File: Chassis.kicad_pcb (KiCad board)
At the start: 4 copper layers, 80 x 80.1 mm, 73 parts, among them IC1 LV2862YDDCR, IC2 RT6285GSP, J1 FR_JST, J10 IN_XT30, J11 SWD_IN, J12 Conn_01x08_Pin, J13 GIM1_JST, J14 GIM2_JST, J15 GIM1_XT30, J16 GIM2_XT30, J17 SWD_OUT, J18 CHA_XT30, J19 SHOO_XT30, J2 BR_JST, J20 GIM_XT30, J21 OUT_JST, J22 5V_XT30, J23 UART_IN, J24 UART_Out, J25 REF_IN, J26 REF_OUT, J27 CAN2_IN, J28 CAN2_OUT, J3 FL_JST, J4 BL_JST, J5 FR_XT30, J6 BR_XT30, J7 FL_XT30, J8 BL_XT30, J9 IN_JST

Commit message: Add le pikja
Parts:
- added G***: LOGO, Robomaster_Special:pikja, B.Cu at (65.0, 94.2)

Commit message: Add names to board
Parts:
- moved G*** 1.13 mm to (111.2, 94.8)
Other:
- board text added: "Bri Dickson Jed Wang Michael Chung"
- board text added: "UT Robomaster Chassis Board"
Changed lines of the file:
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@@
   )
   (footprint "Robomaster_Special:StampedeLogo" (layer "B.Cu")
-    (at 110.4 94 180)
+    (at 111.25 94.75 180)
     (attr board_only exclude_from_pos_files exclude_from_bom)
     (fp_text reference "G***" (at 0 0) (layer "B.SilkS") hide
@@
   (gr_arc (start 48.328427 29.328427) (mid 49.5 26.5) (end 52.328427 25.328427)
     (stroke (width 0.1) (type default)) (layer "Edge.Cuts"))
+  (gr_text "Bri Dickson\nJed Wang\nMichael Chung" (at 104.5 94.25) (layer "B.SilkS")
+    (effects (font (size 1.5 1.5) (thickness 0.1875)) (justify left top mirror))
+  )
+  (gr_text "UT Robomaster\nChassis Board" (at 104.75 93.25) (layer "B.SilkS")
+    (effects (font (size 1.5 1.5) (thickness 0.3) bold italic) (justify left bottom mirror))
+  )
   (gr_text "+19V\n" (at 86.25 61.5 -90) (layer "F.SilkS")
     (effects (font (size 1 1) (thickness 0.15)) (justify right bottom))

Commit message: Add the Roblox face
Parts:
- added G***: LOGO, Robomaster_Special:roblox, B.Cu at (88.2, 65.2)

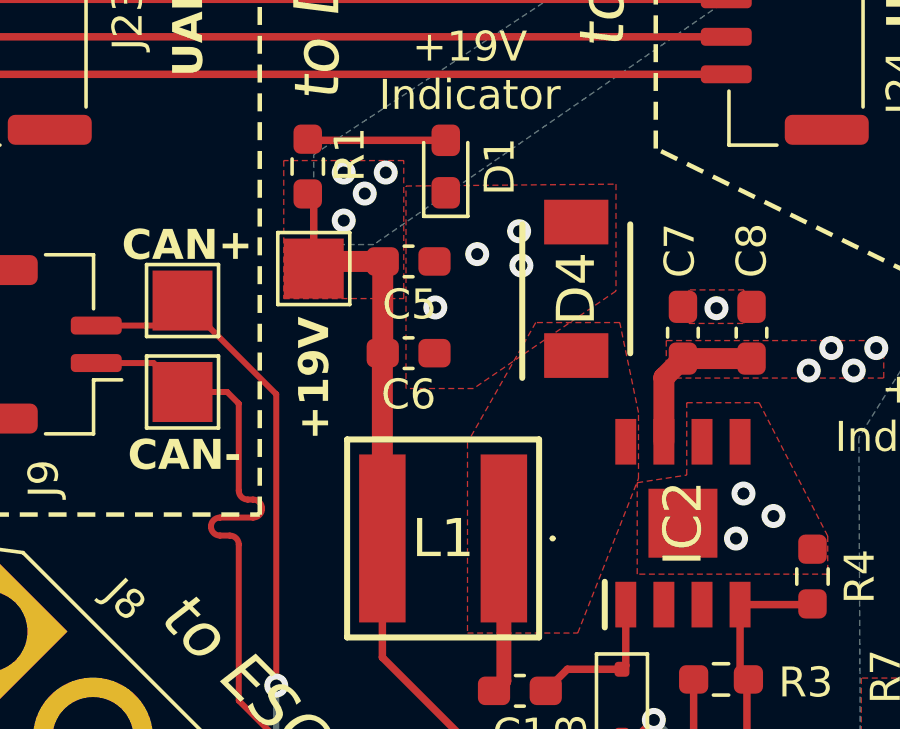
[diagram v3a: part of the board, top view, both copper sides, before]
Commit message: Change output filtering for the +19V to 0805 (Mouser doesn't have 0603)
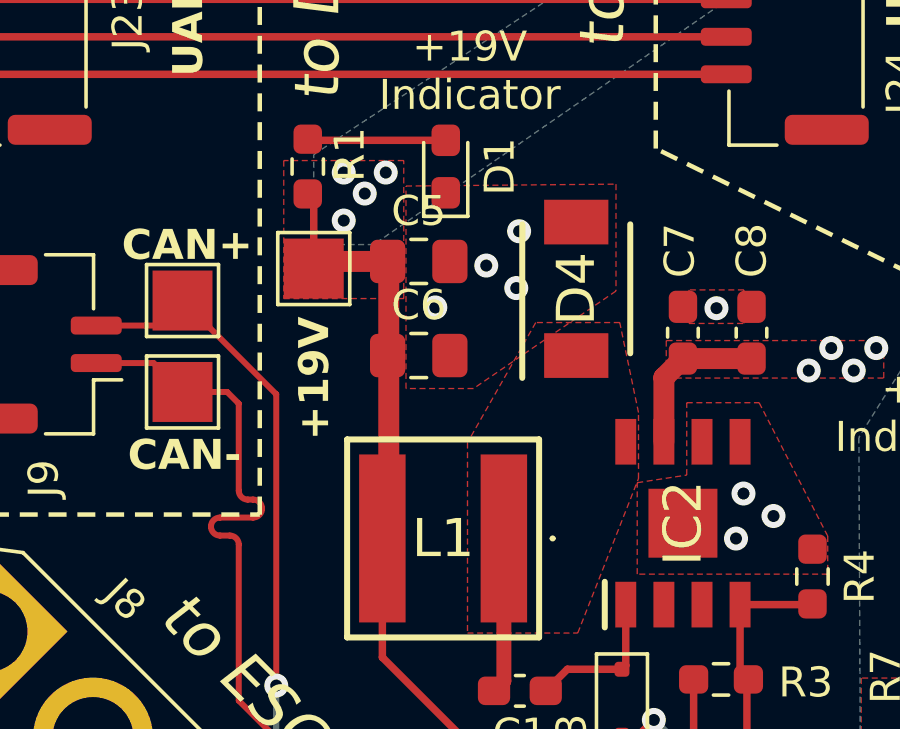
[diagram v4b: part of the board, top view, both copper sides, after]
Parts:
- C5, C6: footprint Capacitor_SMD:C_0603_1608Metric_Pad1.08x0.95mm_HandSolder -> Capacitor_SMD:C_0805_2012Metric_Pad1.18x1.45mm_HandSolder
- moved C6 0.35 mm to (67.5, 81.5)
- moved C5 0.34 mm to (67.5, 78.4)

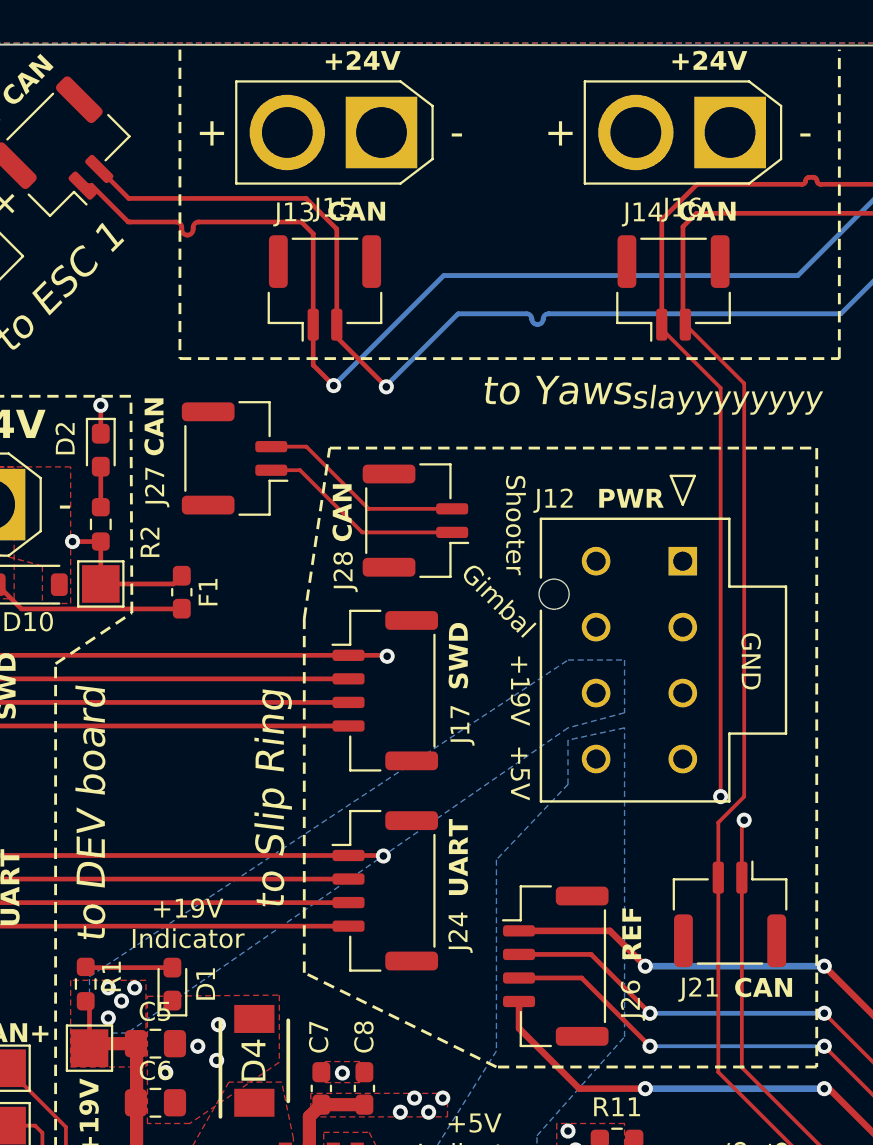
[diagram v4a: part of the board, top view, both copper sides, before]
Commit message: Update footprints + pass DRC
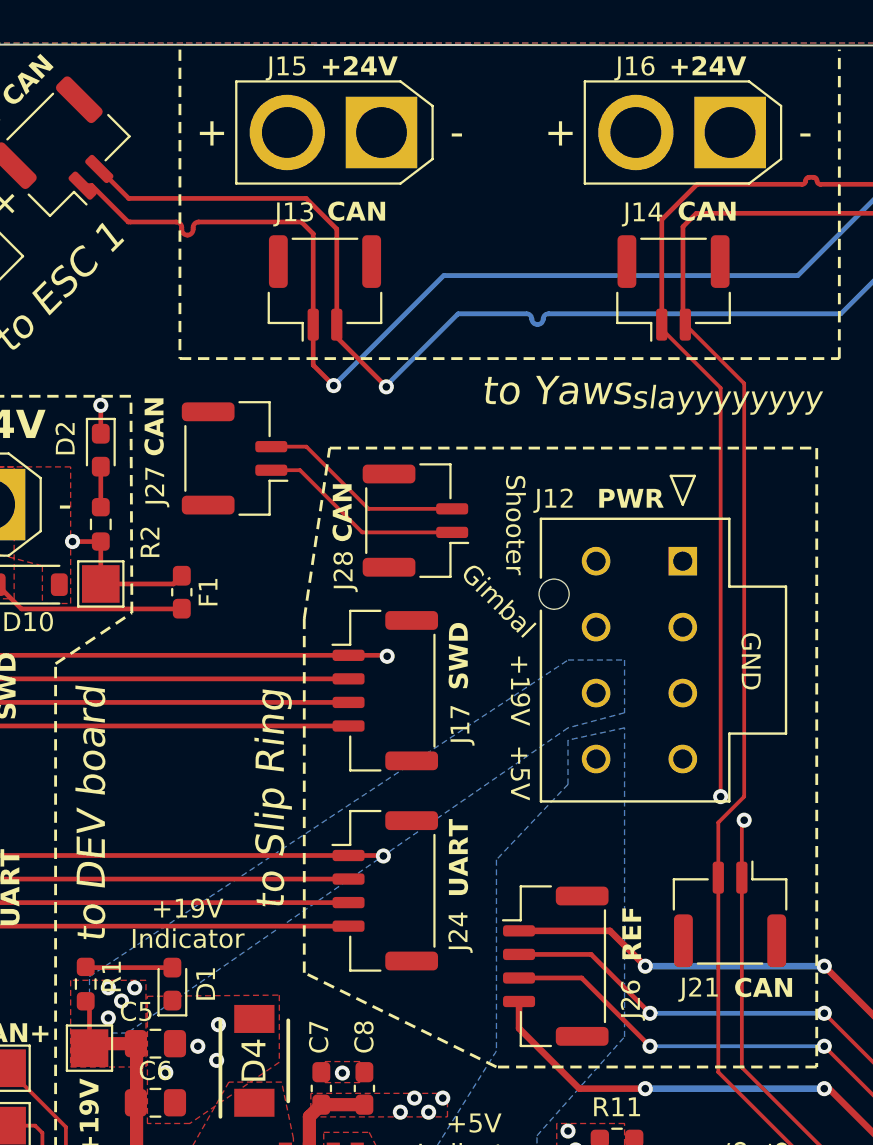
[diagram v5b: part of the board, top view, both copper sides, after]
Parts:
- L1: footprint Robomaster_ICs:MPLAL6060100 -> Robomaster_Passives:MPLAL6060100
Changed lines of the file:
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@@
         (effects (font (size 1 1) (thickness 0.15)))
     )
-    (fp_text user "-" (at -4 0 180) (layer "F.SilkS")
+    (fp_text user "+" (at 9 0 180) (layer "F.SilkS")
         (effects (font (size 1.5 1.5) (thickness 0.15)))
     )
-    (fp_text user "+" (at 9 0 180) (layer "F.SilkS")
+    (fp_text user "-" (at -4 0 180) (layer "F.SilkS")
         (effects (font (size 1.5 1.5) (thickness 0.15)))
     )
@@
         (effects (font (size 1 1) (thickness 0.15)))
     )
-    (fp_text user "-" (at -4 0) (layer "F.SilkS")
+    (fp_text user "+" (at 9 0) (layer "F.SilkS")
         (effects (font (size 1.5 1.5) (thickness 0.15)))
     )
-    (fp_text user "+" (at 9 0) (layer "F.SilkS")
+    (fp_text user "-" (at -4 0) (layer "F.SilkS")
         (effects (font (size 1.5 1.5) (thickness 0.15)))
     )
@@
         (effects (font (size 1 1) (thickness 0.15)))
     )
-    (fp_text user "+" (at 9 0 135) (layer "F.SilkS")
+    (fp_text user "-" (at -4 0 135) (layer "F.SilkS")
         (effects (font (size 1.5 1.5) (thickness 0.15)))
     )
-    (fp_text user "-" (at -4 0 135) (layer "F.SilkS")
+    (fp_text user "+" (at 9 0 135) (layer "F.SilkS")
         (effects (font (size 1.5 1.5) (thickness 0.15)))
     )
@@
       (net 11 "Net-(D8-A)") (pintype "passive"))
     (pad "2" smd roundrect (at 0.9125 0 90) (size 0.975 0.95) (layers "F.Cu" "F.Paste" "F.Mask") (roundrect_rratio 0.25)
-      (net 12 "+24V_Chassis") (pintype "passive") (zone_connect 2))
+      (net 12 "+24V_Chassis") (pintype "passive"))
     (model "${KICAD6_3DMODEL_DIR}/Resistor_SMD.3dshapes/R_0603_1608Metric.wrl"
       (offset (xyz 0 0 0))
@@
         (effects (font (size 1 1) (thickness 0.15)))
     )
-    (fp_text user "1722981108" (at 5.25 -21.620003 -90 unlocked) (layer "F.Fab")
+    (fp_text user "RECOMMENDED_PCB_THICKNESS:_1.60_-_2.40_MM" (at -2.749984 20.929998 -90 unlocked) (layer "Cmts.User")
+        (effects (font (size 1 1) (thickness 0.15)))
+    )
+    (fp_text user "NOTE:" (at -2.749984 14.579998 -90 unlocked) (layer "Cmts.User")
+        (effects (font (size 1 1) (thickness 0.15)))
+    )
+    (fp_text user "MAXIMUM_PACKAGE_HEIGHT:_14_MM" (at -2.749984 18.389998 -90 unlocked) (layer "Cmts.User")
         (effects (font (size 1 1) (thickness 0.15)))
     )
@@
         (effects (font (size 1 1) (thickness 0.15)))
     )
+    (fp_text user "1722981108" (at 5.25 -21.620003 -90 unlocked) (layer "F.Fab")
+        (effects (font (size 1 1) (thickness 0.15)))
+    )
     (fp_text user "${REFERENCE}" (at 5.25 -12.7 -90 unlocked) (layer "F.Fab")
         (effects (font (size 1 1) (thickness 0.15)))
@@
         (effects (font (size 1 1) (thickness 0.15)))
     )
-    (fp_text user "-" (at -4 0 -135) (layer "F.SilkS")
+    (fp_text user "+" (at 9 0 -135) (layer "F.SilkS")
         (effects (font (size 1.5 1.5) (thickness 0.15)))
     )
-    (fp_text user "+" (at 9 0 -135) (layer "F.SilkS")
+    (fp_text user "-" (at -4 0 -135) (layer "F.SilkS")
         (effects (font (size 1.5 1.5) (thickness 0.15)))
     )
@@
         (effects (font (size 1 1) (thickness 0.15)))
     )
-    (fp_text user "-" (at -4 0 180) (layer "F.SilkS")
+    (fp_text user "+" (at 9 0 180) (layer "F.SilkS")
         (effects (font (size 1.5 1.5) (thickness 0.15)))
     )
-    (fp_text user "+" (at 9 0 180) (layer "F.SilkS")
+    (fp_text user "-" (at -4 0 180) (layer "F.SilkS")
         (effects (font (size 1.5 1.5) (thickness 0.15)))
     )
@@
     (pad "9" smd rect (at 0 0 90) (size 2.3 2.3) (layers "F.Cu" "F.Paste" "F.Mask")
       (net 4 "GND") (pinfunction "GND_2") (pintype "passive"))
-    (model "${KICAD_ROBOMASTERS_3DMODEL_DIR}/RT6285GSP.stp"
+    (model "${KICAD_ROBOMASTERS_3DMODEL_DIR}/ICs.3dmodels/RT6285GSP.stp"
       (offset (xyz 0 0 0))
       (scale (xyz 1 1 1))
@@
       (net 19 "+5V") (pinfunction "1") (pintype "passive"))
   )
-  (footprint "Robomaster_ICs:MPLAL6060100" (layer "F.Cu")
+  (footprint "Robomaster_Passives:MPLAL6060100" (layer "F.Cu")
     (at 68.312 87.596 180)
     (descr "6.4x6.6")
@@
     (property "ki_keywords" "inductor choke coil reactor magnetic")
     (attr smd)
-    (fp_text reference "L1" (at 0 0) (layer "F.SilkS")
+    (fp_text reference "L1" (at 0 0 180) (layer "F.SilkS")
         (effects (font (size 1.27 1.27) (thickness 0.254)))
     )
-    (fp_text value "10µH" (at 0 0) (layer "F.SilkS") hide
+    (fp_text value "10µH" (at 0 0 180) (layer "F.SilkS") hide
         (effects (font (size 1.27 1.27) (thickness 0.254)))
     )
-    (fp_text user "${REFERENCE}" (at 0 0) (layer "F.Fab")
+    (fp_text user "${REFERENCE}" (at 0 0 180) (layer "F.Fab")
         (effects (font (size 1.27 1.27) (thickness 0.254)))
     )
@@
     (pad "2" smd rect (at 2.025 0 180) (size 1.55 5.6) (layers "F.Cu" "F.Paste" "F.Mask")
       (net 5 "+19V") (pinfunction "2") (pintype "passive"))
-    (model "${KICAD_ROBOMASTERS_3DMODEL_DIR}/MPL-AL6060-100.stp"
+    (model "${KICAD_ROBOMASTERS_3DMODEL_DIR}/Passives.3dmodels/MPL-AL6060-100.stp"
       (offset (xyz 0 0 0))
       (scale (xyz 1 1 1))
@@
     (property "ki_keywords" "cap capacitor")
     (attr smd)
-    (fp_text reference "C5" (at 0 -1.68) (layer "F.SilkS")
+    (fp_text reference "C5" (at -1 -1.68) (layer "F.SilkS")
         (effects (font (size 1 1) (thickness 0.15)))
     )
@@
     (pad "6" smd rect (at 1.25 -0.95 270) (size 0.6 1.25) (layers "F.Cu" "F.Paste" "F.Mask")
       (net 18 "/24V -> 19V Buck Convertor/SW_{5}") (pinfunction "SW") (pintype "passive"))
-    (model "${KICAD_ROBOMASTERS_3DMODEL_DIR}/LV2862YDDCR.stp"
+    (model "${KICAD_ROBOMASTERS_3DMODEL_DIR}/ICs.3dmodels/LV2862YDDCR.stp"
       (offset (xyz 0 0 0))
       (scale (xyz 1 1 1))
@@
     (property "ki_keywords" "connector")
     (attr through_hole)
-    (fp_text reference "J16" (at 2.5 -4 180) (layer "F.SilkS")
+    (fp_text reference "J16" (at 5 3.5 180) (layer "F.SilkS")
         (effects (font (size 1 1) (thickness 0.15)))
     )
@@
     (property "ki_keywords" "connector")
     (attr through_hole)
-    (fp_text reference "J15" (at 2.5 -4 180) (layer "F.SilkS")
+    (fp_text reference "J15" (at 5 3.5 180) (layer "F.SilkS")
         (effects (font (size 1 1) (thickness 0.15)))
     )
@@
     (effects (font (size 1 1) (thickness 0.15)) (justify left bottom))
   )
-  (gr_text "+24V" (at 94.8 26.8) (layer "F.SilkS")
-    (effects (font (size 1 1) (thickness 0.25) bold) (justify left bottom))
+  (gr_text "+24V" (at 94.75 26.5) (layer "F.SilkS")
+    (effects (font (size 1 1) (thickness 0.25) bold) (justify left))
   )
   (gr_text "CAN" (at 98.2 76) (layer "F.SilkS")
@@
     (effects (font (size 1 1) (thickness 0.15) bold) (justify right bottom))
   )
-  (gr_text "+24V" (at 76.4 26.8) (layer "F.SilkS")
-    (effects (font (size 1 1) (thickness 0.25) bold) (justify left bottom))
+  (gr_text "+24V" (at 76.25 26.5) (layer "F.SilkS")
+    (effects (font (size 1 1) (thickness 0.25) bold) (justify left))
   )
   (gr_text "+24V" (at 123 34.6 -45) (layer "F.SilkS")

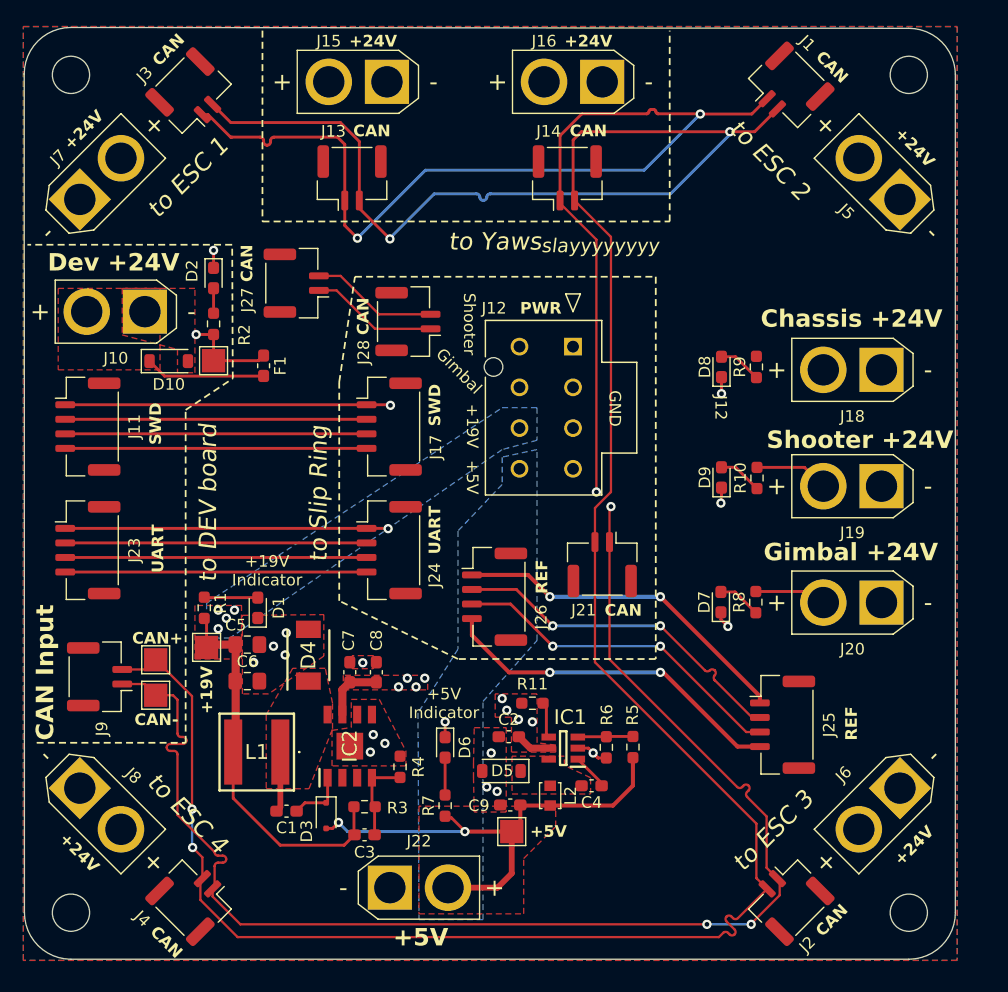
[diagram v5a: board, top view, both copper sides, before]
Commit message: Fix power protection + adj silk
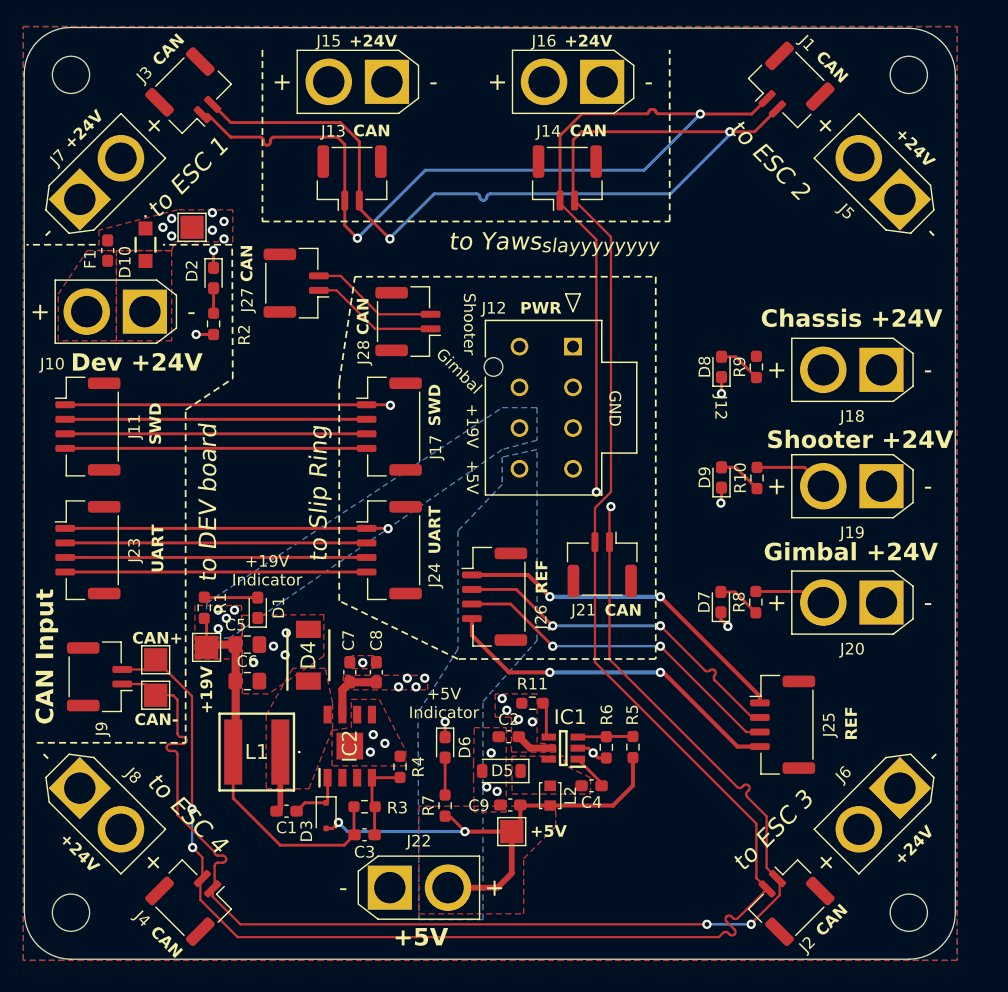
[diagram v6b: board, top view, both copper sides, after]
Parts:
- D10: value TV02W330B-G -> PTVS26VS1UR-QX; footprint Diode_SMD:D_SOD-123 -> Robomaster_Passives:PTVS26VS1URQX
- moved F1 16.7 mm to (55.5, 44.5), turned to 90 degrees
- moved TP3 11.6 mm to (62.8, 42.5)
- moved D10 10.2 mm to (58.8, 44.0), turned to -90 degrees
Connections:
- C2 pad 1: Mini_PC -> +24V
- C7 pad 1: Mini_PC -> +24V
- C8 pad 1: Mini_PC -> +24V
- D10 pad 1: Net-(D10-K) -> +24V
- F1 pad 2: Net-(D10-K) -> +24V
- IC1 pad 5: Mini_PC -> +24V
- IC2 pad 7: Mini_PC -> +24V
- R11 pad 2: Mini_PC -> +24V
- R2 pad 2: Mini_PC -> +24V
- TP3 pad 1: Mini_PC -> +24V
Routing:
- net Mini_PC: track 16.5 -> 0.00 mm, vias 9 -> 0
- net Net-(D10-K): track 10.3 -> 0.00 mm
- net +24V: track 0.00 -> 9.80 mm, vias 0 -> 16
- added copper zone on F.Cu, net +24V
- added copper zone on In2.Cu, net +24V
- removed copper zone on In2.Cu, net Mini_PC
